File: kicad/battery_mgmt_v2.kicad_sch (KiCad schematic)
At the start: 20 parts, among them J301 BATTERY_CONN, Q301 2N7002, U301 BQ25185, U302 TPS7A20

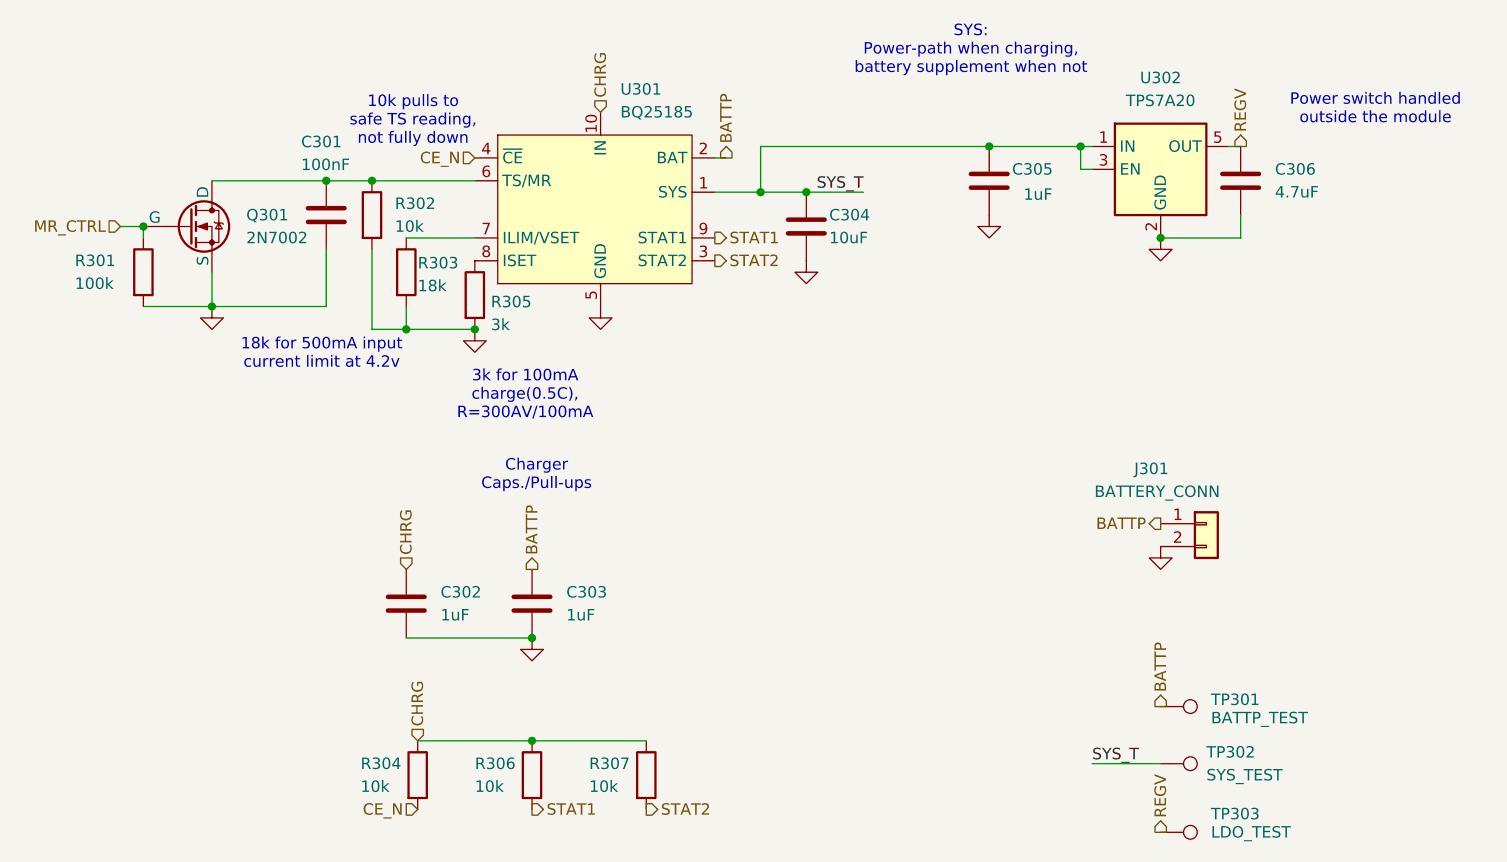
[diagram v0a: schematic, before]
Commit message: Finish PCB component placement
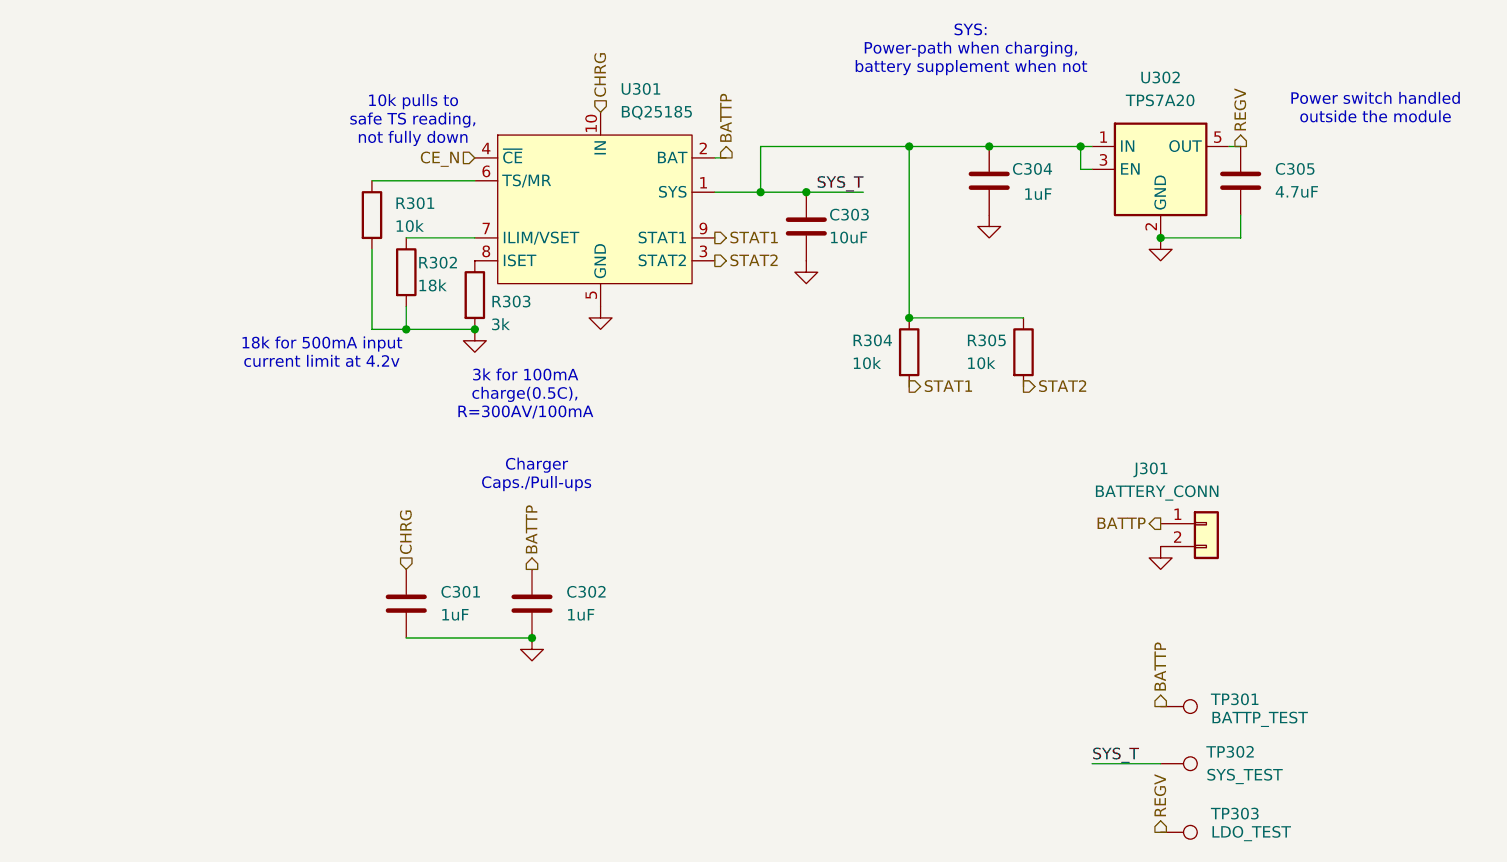
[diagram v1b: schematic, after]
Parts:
- removed C301: 100nF, Capacitor_SMD:C_0402_1005Metric, symbol Device:C
- removed Q301: 2N7002, Package_TO_SOT_SMD:SOT-23-3, symbol Simulation_SPICE:NMOS
- removed R301: 100k, Resistor_SMD:R_0402_1005Metric, symbol Device:R
- removed R304: 10k, Resistor_SMD:R_0402_1005Metric, symbol Device:R
- renumbered C302 to C301, C303 to C302, C304 to C303, C305 to C304, C306 to C305, R302 to R301, R303 to R302, R305 to R303, R306 to R304, R307 to R305
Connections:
- net CHRG: no longer R304.1, R305.1
- net SYS_T: now also R304.1, R305.1
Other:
- moved on the sheet: R304, R305

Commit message: Minor schematic fixes and PCB trace progress
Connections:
- net SYS_T: no longer R304.1, R305.1
- new net +3.3V: R304.1, R305.1
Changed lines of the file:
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@@
+	)
+	(junction
+		(at 151.13 71.12)
+		(diameter 0)
+		(color 0 0 0 0)
+	)
+	(junction
+		(at 146.05 71.12)
+		(diameter 0)
+		(color 0 0 0 0)
+	)
+	(junction
+		(at 190.5 76.2)
+		(diameter 0)
+		(color 0 0 0 0)
+	)
+	(junction
+		(at 171.45 66.04)
+		(diameter 0)
+		(color 0 0 0 0)
+	)
+	(junction
+		(at 106.68 86.36)
+		(diameter 0)
+		(color 0 0 0 0)
+	)
+	(junction
+		(at 114.3 86.36)
+		(diameter 0)
+		(color 0 0 0 0)
+	)
+	(junction
+		(at 120.65 120.65)
+		(diameter 0)
+		(color 0 0 0 0)
 	)
 	(junction
@@
 	)
 	(junction
-		(at 151.13 71.12)
-		(diameter 0)
-		(color 0 0 0 0)
-	)
-	(junction
-		(at 146.05 71.12)
-		(diameter 0)
-		(color 0 0 0 0)
-	)
-	(junction
-		(at 190.5 76.2)
-		(diameter 0)
-		(color 0 0 0 0)
-	)
-	(junction
-		(at 171.45 66.04)
-		(diameter 0)
-		(color 0 0 0 0)
-	)
-	(junction
-		(at 106.68 86.36)
-		(diameter 0)
-		(color 0 0 0 0)
-	)
-	(junction
-		(at 114.3 86.36)
-		(diameter 0)
-		(color 0 0 0 0)
-	)
-	(junction
-		(at 120.65 120.65)
-		(diameter 0)
-		(color 0 0 0 0)
-	)
-	(junction
 		(at 181.61 66.04)
 		(diameter 0)
 		(color 0 0 0 0)
 	)
-	(junction
-		(at 162.56 66.04)
-		(diameter 0)
-		(color 0 0 0 0)
-	)
-	(wire
-		(pts
-			(xy 162.56 66.04) (xy 162.56 85.09)
-		)
-		(stroke
-			(width 0)
-			(type default)
-		)
-	)
-	(wire
-		(pts
-			(xy 162.56 66.04) (xy 171.45 66.04)
+	(wire
+		(pts
+			(xy 146.05 66.04) (xy 171.45 66.04)
 		)
 		(stroke
@@
 		(pts
 			(xy 162.56 85.09) (xy 175.26 85.09)
-		)
-		(stroke
-			(width 0)
-			(type default)
-		)
-	)
-	(wire
-		(pts
-			(xy 146.05 66.04) (xy 162.56 66.04)
 		)
 		(stroke
@@
 					(unit 1)
 				)
+			)
+		)
+	)
+	(symbol
+		(lib_id "power:+3.3V")
+		(at 162.56 85.09 0)
+		(unit 1)
+		(exclude_from_sim no)
+		(in_bom yes)
+		(on_board yes)
+		(dnp no)
+		(fields_autoplaced yes)
+		(property "Reference" "#PWR0308"
+			(at 162.56 88.9 0)
+			(effects
+				(font
+					(size 1.27 1.27)
+				)
+				(hide yes)
+			)
+		)
+		(property "Value" "+3.3V"
+			(at 162.56 80.01 0)
+			(effects
+				(font
+					(size 1.27 1.27)
+				)
+			)
+		)
+		(property "Footprint" ""
+			(at 162.56 85.09 0)
+			(effects
+				(font
+					(size 1.27 1.27)
+				)
+				(hide yes)
+			)
+		)
+		(property "Datasheet" ""
+			(at 162.56 85.09 0)
+			(effects
+				(font
+					(size 1.27 1.27)
+				)
+				(hide yes)
+			)
+		)
+		(property "Description" "Power symbol creates a global label with name \"+3.3V\""
+			(at 162.56 85.09 0)
+			(effects
+				(font
+					(size 1.27 1.27)
+				)
+				(hide yes)
+			)
+		)
+		(pin "1"
+		)
+		(instances
+			(project "kicad"
+				(path "/97e37379-fec6-4f0d-82d9-4ea53516bb02/d2226d13-9ee7-410c-817d-a66f223af34c"
+					(reference "#PWR0308")
+					(unit 1)
+				)

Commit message: Finish silkscreen
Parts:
- removed TP301: BATTP_TEST, TestPoint:TestPoint_Pad_D1.0mm, symbol Connector:TestPoint
- removed TP302: SYS_TEST, TestPoint:TestPoint_Pad_D1.0mm, symbol Connector:TestPoint
- removed TP303: LDO_TEST, TestPoint:TestPoint_Pad_D1.0mm, symbol Connector:TestPoint

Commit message: start v3, complete pcb restart and remove haptics
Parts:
- renumbered C304 to C301, C305 to C302, C301 to C304, C302 to C305
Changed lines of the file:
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@@
 (kicad_sch
-	(version 20231120)
+	(version 20250114)
 	(generator "eeschema")
-	(generator_version "8.0")
+	(generator_version "9.0")
 	(paper "A4")
 	(title_block
@@
 		(comment 1 "Lucas Merritt")
 	)
+	(text "SYS:\nPower-path when charging,\nbattery supplement when not"
+		(exclude_from_sim no)
+		(at 169.418 55.372 0)
+		(effects
+			(font
+				(size 1.27 1.27)
+			)
+		)
+	)
+	(text "3k for 100mA\ncharge(0.5C),\nR=300AV/100mA"
+		(exclude_from_sim no)
+		(at 119.888 93.726 0)
+		(effects
+			(font
+				(size 1.27 1.27)
+			)
+		)
+	)
+	(text "Power switch handled\noutside the module"
+		(exclude_from_sim no)
+		(at 214.376 61.976 0)
+		(effects
+			(font
+				(size 1.27 1.27)
+			)
+		)
+	)
+	(text "10k pulls to\nsafe TS reading,\nnot fully down"
+		(exclude_from_sim no)
+		(at 107.442 63.246 0)
+		(effects
+			(font
+				(size 1.27 1.27)
+			)
+		)
+	)
+	(text "Charger\nCaps./Pull-ups"
+		(exclude_from_sim no)
+		(at 121.158 102.616 0)
+		(effects
+			(font
+				(size 1.27 1.27)
+			)
+		)
+	)
+	(text "18k for 500mA input\ncurrent limit at 4.2v"
+		(exclude_from_sim no)
+		(at 97.282 89.154 0)
+		(effects
+			(font
+				(size 1.27 1.27)
+			)
+		)
+	)
 	(junction
 		(at 151.13 71.12)
@@
 		)
 	)
-	(text "SYS:\nPower-path when charging,\nbattery supplement when not"
-		(exclude_from_sim no)
-		(at 169.418 55.372 0)
+	(label "SYS_T"
+		(at 157.48 71.12 180)
 		(effects
 			(font
 				(size 1.27 1.27)
 			)
-		)
-	)
-	(text "3k for 100mA\ncharge(0.5C),\nR=300AV/100mA"
-		(exclude_from_sim no)
-		(at 119.888 93.726 0)
+			(justify right bottom)
+		)
+	)
+	(hierarchical_label "CHRG"
+		(shape input)
+		(at 128.27 62.23 90)
 		(effects
 			(font
 				(size 1.27 1.27)
 			)
-		)
-	)
-	(text "Power switch handled\noutside the module"
-		(exclude_from_sim no)
-		(at 214.376 61.976 0)
+			(justify left)
+		)
+	)
+	(hierarchical_label "BATTP"
+		(shape output)
+		(at 142.24 67.31 90)
 		(effects
 			(font
 				(size 1.27 1.27)
 			)
-		)
-	)
-	(text "10k pulls to\nsafe TS reading,\nnot fully down"
-		(exclude_from_sim no)
-		(at 107.442 63.246 0)
+			(justify left)
+		)
+	)
+	(hierarchical_label "BATTP"
+		(shape output)
+		(at 190.5 107.95 180)
 		(effects
 			(font
 				(size 1.27 1.27)
 			)
-		)
-	)
-	(text "Charger\nCaps./Pull-ups"
-		(exclude_from_sim no)
-		(at 121.158 102.616 0)
+			(justify right)
+		)
+	)
+	(hierarchical_label "STAT2"
+		(shape output)
+		(at 140.97 78.74 0)
 		(effects
 			(font
 				(size 1.27 1.27)
 			)
-		)
-	)
-	(text "18k for 500mA input\ncurrent limit at 4.2v"
-		(exclude_from_sim no)
-		(at 97.282 89.154 0)
+			(justify left)
+		)
+	)
+	(hierarchical_label "STAT2"
+		(shape output)
+		(at 175.26 92.71 0)
 		(effects
 			(font
 				(size 1.27 1.27)
 			)
-		)
-	)
-	(label "SYS_T"
-		(at 157.48 71.12 180)
-		(fields_autoplaced yes)
+			(justify left)
+		)
+	)
+	(hierarchical_label "STAT1"
+		(shape output)
+		(at 140.97 76.2 0)
 		(effects
 			(font
 				(size 1.27 1.27)
 			)
-			(justify right bottom)
-		)
-	)
-	(hierarchical_label "CHRG"
-		(shape input)
-		(at 128.27 62.23 90)
-		(fields_autoplaced yes)
+			(justify left)
+		)
+	)
+	(hierarchical_label "REGV"
+		(shape output)
+		(at 199.39 66.04 90)
 		(effects
 			(font
@@
 		)
 	)
-	(hierarchical_label "BATTP"
-		(shape output)
-		(at 142.24 67.31 90)
-		(fields_autoplaced yes)
+	(hierarchical_label "CE_N"
+		(shape input)
+		(at 114.3 67.31 180)
 		(effects
 			(font
 				(size 1.27 1.27)
 			)
-			(justify left)
+			(justify right)
 		)
 	)
 	(hierarchical_label "BATTP"
 		(shape output)
-		(at 190.5 107.95 180)
-		(fields_autoplaced yes)
+		(at 120.65 113.03 90)
 		(effects
 			(font
 				(size 1.27 1.27)
 			)
-			(justify right)
-		)
-	)
-	(hierarchical_label "STAT2"
+			(justify left)
+		)
+	)
+	(hierarchical_label "STAT1"
 		(shape output)
-		(at 140.97 78.74 0)
-		(fields_autoplaced yes)
+		(at 162.56 92.71 0)
 		(effects
 			(font
@@
 		)
 	)
-	(hierarchical_label "STAT2"
-		(shape output)
-		(at 175.26 92.71 0)
-		(fields_autoplaced yes)
+	(hierarchical_label "CHRG"
+		(shape input)
+		(at 106.68 113.03 90)
 		(effects
 			(font
@@
 		)
 	)
-	(hierarchical_label "STAT1"
-		(shape output)
-		(at 140.97 76.2 0)
-		(fields_autoplaced yes)
-		(effects
-			(font
-				(size 1.27 1.27)
-			)
-			(justify left)
-		)
-	)
-	(hierarchical_label "REGV"
-		(shape output)
-		(at 199.39 66.04 90)
-		(fields_autoplaced yes)
-		(effects
-			(font
-				(size 1.27 1.27)
-			)
-			(justify left)
-		)
-	)
-	(hierarchical_label "CE_N"
-		(shape input)
-		(at 114.3 67.31 180)
-		(fields_autoplaced yes)
-		(effects
-			(font
-				(size 1.27 1.27)
-			)
-			(justify right)
-		)
-	)
-	(hierarchical_label "BATTP"
-		(shape output)
-		(at 120.65 113.03 90)
-		(fields_autoplaced yes)
-		(effects
-			(font
-				(size 1.27 1.27)
-			)
-			(justify left)
-		)
-	)
-	(hierarchical_label "STAT1"
-		(shape output)
-		(at 162.56 92.71 0)
-		(fields_autoplaced yes)
-		(effects
-			(font
-				(size 1.27 1.27)
-			)
-			(justify left)
-		)
-	)
-	(hierarchical_label "CHRG"
-		(shape input)
-		(at 106.68 113.03 90)
-		(fields_autoplaced yes)
-		(effects
-			(font
-				(size 1.27 1.27)
-			)
-			(justify left)
-		)
-	)
 	(symbol
 		(lib_id "Device:C")
@@
 		(dnp no)
 		(fields_autoplaced yes)
-		(property "Reference" "#PWR0305"
+		(property "Reference" "#PWR0301"
 			(at 171.45 80.01 0)
 			(effects
@@
 			(project "kicad"
 				(path "/97e37379-fec6-4f0d-82d9-4ea53516bb02/d2226d13-9ee7-410c-817d-a66f223af34c"
-					(reference "#PWR0305")
+					(reference "#PWR0301")
 					(unit 1)
 				)
@@
 		(dnp no)
 		(fields_autoplaced yes)
-		(property "Reference" "C305"
+		(property "Reference" "C302"
 			(at 203.2 68.5799 0)
 			(effects
@@
 			(project "kicad"
 				(path "/97e37379-fec6-4f0d-82d9-4ea53516bb02/d2226d13-9ee7-410c-817d-a66f223af34c"
-					(reference "C305")
+					(reference "C302")
 					(unit 1)
 				)
@@
 		(dnp no)
 		(fields_autoplaced yes)
-		(property "Reference" "#PWR0306"
+		(property "Reference" "#PWR0302"
 			(at 190.5 82.55 0)
 			(effects
@@
 			(project "kicad"
 				(path "/97e37379-fec6-4f0d-82d9-4ea53516bb02/d2226d13-9ee7-410c-817d-a66f223af34c"
-					(reference "#PWR0306")
+					(reference "#PWR0302")
 					(unit 1)
 				)
@@
 		(dnp no)
 		(fields_autoplaced yes)
-		(property "Reference" "C302"
+		(property "Reference" "C305"
 			(at 124.46 115.5699 0)
 			(effects
@@
 			(project "kicad"
 				(path "/97e37379-fec6-4f0d-82d9-4ea53516bb02/d2226d13-9ee7-410c-817d-a66f223af34c"
-					(reference "C302")
+					(reference "C305")
 					(unit 1)
 				)
@@
 		(dnp no)
 		(fields_autoplaced yes)
-		(property "Reference" "C301"
+		(property "Reference" "C304"
 			(at 110.49 115.5699 0)
 			(effects
@@
 			(project "kicad"
 				(path "/97e37379-fec6-4f0d-82d9-4ea53516bb02/d2226d13-9ee7-410c-817d-a66f223af34c"
-					(reference "C301")
+					(reference "C304")
 					(unit 1)
 				)
@@
 		(dnp no)
 		(fields_autoplaced yes)
-		(property "Reference" "#PWR0308"
+		(property "Reference" "#PWR0305"
 			(at 162.56 88.9 0)
 			(effects
@@
 			(project "kicad"
 				(path "/97e37379-fec6-4f0d-82d9-4ea53516bb02/d2226d13-9ee7-410c-817d-a66f223af34c"
-					(reference "#PWR0308")
+					(reference "#PWR0305")
 					(unit 1)
 				)
@@
 		(on_board yes)
 		(dnp no)
-		(property "Reference" "C304"
+		(property "Reference" "C301"
 			(at 173.99 68.58 0)
 			(effects
@@
 			(project "kicad"
 				(path "/97e37379-fec6-4f0d-82d9-4ea53516bb02/d2226d13-9ee7-410c-817d-a66f223af34c"
-					(reference "C304")
+					(reference "C301")
 					(unit 1)
 				)
@@
 		(dnp no)
 		(fields_autoplaced yes)
-		(property "Reference" "#PWR0303"
+		(property "Reference" "#PWR0304"
 			(at 128.27 90.17 0)
 			(effects
@@
 			(project "kicad"
 				(path "/97e37379-fec6-4f0d-82d9-4ea53516bb02/d2226d13-9ee7-410c-817d-a66f223af34c"
-					(reference "#PWR0303")
+					(reference "#PWR0304")
 					(unit 1)
 				)
@@
 		(dnp no)
 		(fields_autoplaced yes)
-		(property "Reference" "#PWR0302"
+		(property "Reference" "#PWR0308"
 			(at 120.65 127 0)
 			(effects
@@
 			(project "kicad"
 				(path "/97e37379-fec6-4f0d-82d9-4ea53516bb02/d2226d13-9ee7-410c-817d-a66f223af34c"
-					(reference "#PWR0302")
+					(reference "#PWR0308")
 					(unit 1)
 				)
@@
 		(dnp no)
 		(fields_autoplaced yes)
-		(property "Reference" "#PWR0304"
+		(property "Reference" "#PWR0303"
 			(at 151.13 85.09 0)
 			(effects
@@
 			(project "kicad"
 				(path "/97e37379-fec6-4f0d-82d9-4ea53516bb02/d2226d13-9ee7-410c-817d-a66f223af34c"
-					(reference "#PWR0304")
+					(reference "#PWR0303")
 					(unit 1)
 				)
@@
 		(dnp no)
 		(fields_autoplaced yes)
-		(property "Reference" "#PWR0301"
+		(property "Reference" "#PWR0306"
 			(at 114.3 92.71 0)
 			(effects
@@
 			(project "kicad"
 				(path "/97e37379-fec6-4f0d-82d9-4ea53516bb02/d2226d13-9ee7-410c-817d-a66f223af34c"
-					(reference "#PWR0301")
-					(unit 1)
-				)
+					(reference "#PWR0306")
+					(unit 1)
+				)
